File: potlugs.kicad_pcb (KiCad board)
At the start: 2 copper layers, 10 x 15 mm, 2 parts, among them J1 640456-3

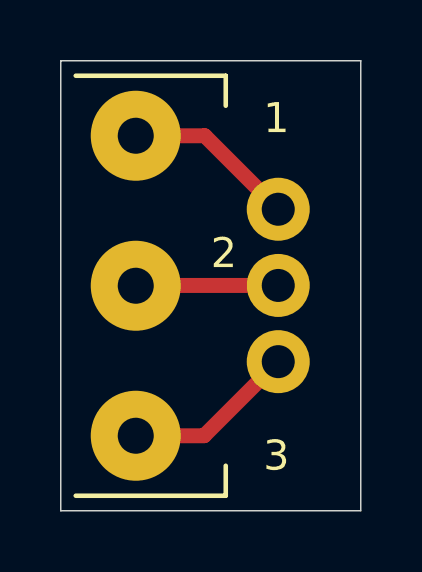
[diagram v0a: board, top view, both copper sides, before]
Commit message: Revert "Make board bigger and remove bevels."
This reverts commit c6e11588c159b63a6cef385ffa4c164769ff8ee9.
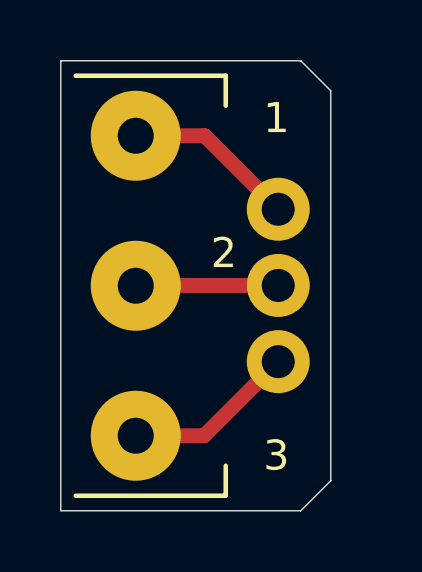
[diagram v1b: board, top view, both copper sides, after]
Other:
- board size 10 x 15 mm -> 9 x 15 mm
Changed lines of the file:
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@@
 	)
 	(gr_line
-		(start 155.25 109.25)
-		(end 155.25 94.25)
+		(start 154.25 108.25)
+		(end 154.25 95.25)
 		(stroke
 			(width 0.05)
@@
 	(gr_line
 		(start 145.25 109.25)
-		(end 155.25 109.25)
+		(end 153.25 109.25)
 		(stroke
 			(width 0.05)
@@
 	)
 	(gr_line
-		(start 145.25 94.25)
-		(end 155.25 94.25)
+		(start 153.25 94.25)
+		(end 154.25 95.25)
 		(stroke
 			(width 0.05)
+			(type default)
+		)
+		(layer "Edge.Cuts")
+	)
+	(gr_line
+		(start 145.25 94.25)
+		(end 153.25 94.25)
+		(stroke
+			(width 0.05)
+			(type default)
+		)
+		(layer "Edge.Cuts")
+	)
+	(gr_line
+		(start 153.25 109.25)
+		(end 154.25 108.25)
+		(stroke
+			(width 0.05)

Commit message: Make board bigger and remove bevels.
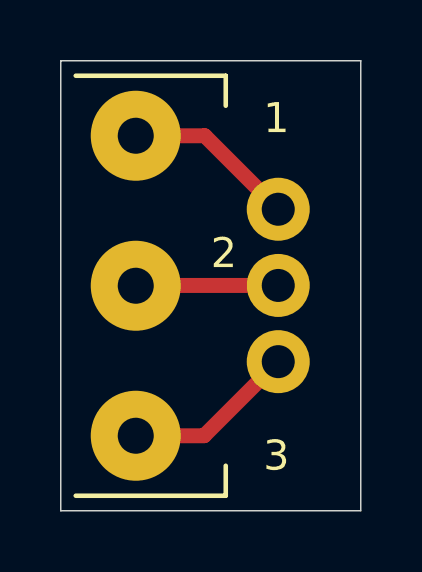
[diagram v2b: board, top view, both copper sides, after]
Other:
- board size 9 x 15 mm -> 10 x 15 mm
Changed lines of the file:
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@@
 	)
 	(gr_line
-		(start 154.25 108.25)
-		(end 154.25 95.25)
+		(start 155.25 109.25)
+		(end 155.25 94.25)
 		(stroke
 			(width 0.05)
@@
 	(gr_line
 		(start 145.25 109.25)
-		(end 153.25 109.25)
+		(end 155.25 109.25)
 		(stroke
 			(width 0.05)
@@
 	)
 	(gr_line
-		(start 153.25 94.25)
-		(end 154.25 95.25)
+		(start 145.25 94.25)
+		(end 155.25 94.25)
 		(stroke
 			(width 0.05)
-			(type default)
-		)
-		(layer "Edge.Cuts")
-	)
-	(gr_line
-		(start 145.25 94.25)
-		(end 153.25 94.25)
-		(stroke
-			(width 0.05)
-			(type default)
-		)
-		(layer "Edge.Cuts")
-	)
-	(gr_line
-		(start 153.25 109.25)
-		(end 154.25 108.25)
-		(stroke
-			(width 0.05)
